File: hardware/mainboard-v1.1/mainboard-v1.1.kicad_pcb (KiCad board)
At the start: 2 copper layers, 86 x 62 mm, 27 parts, among them J1 Conn_01x01, J2 Conn_01x01, J3 Conn_01x03, J4 Conn_01x03, J5 Conn_01x05, SW1 SW_SPDT, SW2 SW_SPST, SW3 SW_SPST, SW4 SW_SPST, SW5 SW_SPST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

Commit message: pcb update for v1.1
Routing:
- net /SERVO1: track 42.3 -> 46.6 mm
- net /SERVO2: track 42.3 -> 41.1 mm
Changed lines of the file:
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@@
     (fp_arc (start 10.726537 -0.155903) (mid 11.428136 -0.857503) (end 12.129736 -0.155903)
       (stroke (width 0.25) (type solid)) (layer "Dwgs.User"))
-    (fp_arc (start 11.740267 -36.934704) (mid 12.447516 -36.641667) (end 12.740267 -35.934303)
+    (fp_arc (start 11.740267 -36.934704) (mid 12.447538 -36.641681) (end 12.740267 -35.934303)
       (stroke (width 0.25) (type solid)) (layer "Dwgs.User"))
     (fp_arc (start 12.716687 22.847905) (mid 12.42365 23.554745) (end 11.716687 23.847504)
@@
   (segment (start 134.5 74.8) (end 136.45 74.8) (width 0.25) (layer "F.Cu") (net 2))
   (via (at 136.5 74.8) (size 0.8) (drill 0.4) (layers "F.Cu" "B.Cu") (net 2))
-  (segment (start 121.81 78.19) (end 121.81 77.94) (width 0.5) (layer "B.Cu") (net 2))
+  (segment (start 126.5 73.25) (end 135.85 73.25) (width 0.5) (layer "B.Cu") (net 2))
+  (segment (start 136.5 73.9) (end 136.5 74.8) (width 0.5) (layer "B.Cu") (net 2))
   (segment (start 114 78) (end 121.62 78) (width 0.5) (layer "B.Cu") (net 2))
-  (segment (start 126.5 73.25) (end 136.25 73.25) (width 0.5) (layer "B.Cu") (net 2))
   (segment (start 121.62 78) (end 121.81 78.19) (width 0.5) (layer "B.Cu") (net 2))
   (segment (start 171 81.25) (end 171 78) (width 0.5) (layer "B.Cu") (net 2))
@@
   (segment (start 125.49 87.25) (end 165 87.25) (width 0.5) (layer "B.Cu") (net 2))
   (segment (start 121.81 83.57) (end 121.81 78.19) (width 0.5) (layer "B.Cu") (net 2))
+  (segment (start 121.81 77.94) (end 126.5 73.25) (width 0.5) (layer "B.Cu") (net 2))
+  (segment (start 121.81 78.19) (end 121.81 77.94) (width 0.5) (layer "B.Cu") (net 2))
   (segment (start 121.81 83.57) (end 125.49 87.25) (width 0.5) (layer "B.Cu") (net 2))
-  (segment (start 136.25 73.25) (end 136.5 73.5) (width 0.5) (layer "B.Cu") (net 2))
-  (segment (start 121.81 77.94) (end 126.5 73.25) (width 0.5) (layer "B.Cu") (net 2))
-  (segment (start 136.5 73.5) (end 136.5 74.8) (width 0.5) (layer "B.Cu") (net 2))
+  (segment (start 135.85 73.25) (end 136.5 73.9) (width 0.5) (layer "B.Cu") (net 2))
   (segment (start 111.5 78) (end 115.282934 81.782934) (width 0.25) (layer "F.Cu") (net 3))
   (segment (start 115.282934 81.782934) (end 123.782934 81.782934) (width 0.25) (layer "F.Cu") (net 3))
@@
   (segment (start 163.5 86) (end 168.5 81) (width 0.25) (layer "F.Cu") (net 5))
   (segment (start 168.5 81) (end 168.5 78) (width 0.25) (layer "F.Cu") (net 5))
-  (segment (start 132.8 74.8) (end 132.75 74.75) (width 0.25) (layer "F.Cu") (net 6))
-  (segment (start 132.75 76) (end 131.97 76.78) (width 0.5) (layer "F.Cu") (net 6))
-  (segment (start 132.75 74.75) (end 132.75 76) (width 0.5) (layer "F.Cu") (net 6))
-  (segment (start 131.97 76.78) (end 131.97 83.57) (width 0.5) (layer "F.Cu") (net 6))
-  (segment (start 133 74.8) (end 132.8 74.8) (width 0.25) (layer "F.Cu") (net 6))
+  (segment (start 132.8 75.9) (end 131.97 76.73) (width 0.5) (layer "F.Cu") (net 6))
+  (segment (start 133 75.7) (end 133 74.8) (width 0.25) (layer "F.Cu") (net 6))
+  (segment (start 132.8 75.9) (end 133 75.7) (width 0.25) (layer "F.Cu") (net 6))
+  (segment (start 131.97 76.73) (end 131.97 83.57) (width 0.5) (layer "F.Cu") (net 6))
   (segment (start 134.5 73) (end 134 73.5) (width 0.25) (layer "F.Cu") (net 7))
   (segment (start 134 73.5) (end 134 74.8) (width 0.25) (layer "F.Cu") (net 7))
-  (segment (start 134 75.30962) (end 137.05 78.35962) (width 0.25) (layer "F.Cu") (net 7))
-  (segment (start 134 74.8) (end 134 75.30962) (width 0.25) (layer "F.Cu") (net 7))
+  (segment (start 134.025 74.825) (end 134.025 75.33462) (width 0.25) (layer "F.Cu") (net 7))
   (segment (start 137.05 78.35962) (end 137.05 83.57) (width 0.25) (layer "F.Cu") (net 7))
+  (segment (start 134 74.8) (end 134.025 74.825) (width 0.25) (layer "F.Cu") (net 7))
   (segment (start 134.5 71.7) (end 134.5 73) (width 0.25) (layer "F.Cu") (net 7))
+  (segment (start 134.025 75.33462) (end 137.05 78.35962) (width 0.25) (layer "F.Cu") (net 7))
   (segment (start 159.49 62.225) (end 159.49 76.26) (width 0.25) (layer "F.Cu") (net 11))
   (segment (start 153.75 80.05) (end 153.75 80.75) (width 1) (layer "F.Cu") (net 11))
@@
   (segment (start 130.25 116.5) (end 130.25 110) (width 0.25) (layer "F.Cu") (net 14))
   (segment (start 129.43 109.18) (end 130.25 110) (width 0.25) (layer "F.Cu") (net 14))
-  (segment (start 133.5 76) (end 133.5 75.622793) (width 0.5) (layer "F.Cu") (net 15))
-  (segment (start 133.5 74.8) (end 133.5 75.5) (width 0.25) (layer "F.Cu") (net 15))
-  (segment (start 134.51 77.01) (end 133.5 76) (width 0.5) (layer "F.Cu") (net 15))
-  (segment (start 134.51 83.57) (end 134.51 77.01) (width 0.5) (layer "F.Cu") (net 15))
+  (segment (start 134.51 76.76) (end 134.51 83.57) (width 0.5) (layer "F.Cu") (net 15))
+  (segment (start 133.75 76) (end 134.51 76.76) (width 0.5) (layer "F.Cu") (net 15))
+  (segment (start 133.75 76) (end 133.5 75.75) (width 0.25) (layer "F.Cu") (net 15))
+  (segment (start 133.5 75.75) (end 133.5 74.8) (width 0.25) (layer "F.Cu") (net 15))
   (segment (start 139.59 79.41) (end 151.08 67.92) (width 0.5) (layer "F.Cu") (net 16))
   (segment (start 139.59 83.57) (end 139.59 79.41) (width 0.5) (layer "F.Cu") (net 16))
   (segment (start 151.08 67.92) (end 151.08 64) (width 0.5) (layer "F.Cu") (net 16))
-  (segment (start 163.75 60) (end 164.57 60.82) (width 0.5) (layer "B.Cu") (net 16))
-  (segment (start 164.57 60.82) (end 164.57 62.225) (width 0.5) (layer "B.Cu") (net 16))
-  (segment (start 153.25 60) (end 163.75 60) (width 0.5) (layer "B.Cu") (net 16))
-  (segment (start 151.08 62.17) (end 153.25 60) (width 0.5) (layer "B.Cu") (net 16))
-  (segment (start 151.08 64) (end 151.08 62.17) (width 0.5) (layer "B.Cu") (net 16))
+  (segment (start 152.78 65.7) (end 163.1 65.7) (width 0.5) (layer "B.Cu") (net 16))
+  (segment (start 164.57 64.23) (end 164.57 62.225) (width 0.5) (layer "B.Cu") (net 16))
+  (segment (start 163.1 65.7) (end 164.57 64.23) (width 0.5) (layer "B.Cu") (net 16))
+  (segment (start 151.08 64) (end 152.78 65.7) (width 0.5) (layer "B.Cu") (net 16))
   (segment (start 136.5 71.25) (end 136 70.75) (width 0.25) (layer "F.Cu") (net 17))
   (segment (start 133.9 64.1) (end 133.9 71.55) (width 0.5) (layer "F.Cu") (net 17))
@@
   (segment (start 133.5 71.7) (end 134 71.7) (width 0.25) (layer "F.Cu") (net 17))
   (via (at 136 70.75) (size 0.8) (drill 0.4) (layers "F.Cu" "B.Cu") (net 17))
-  (segment (start 155.75 70.75) (end 162.03 64.47) (width 0.25) (layer "B.Cu") (net 17))
-  (segment (start 136 70.75) (end 155.75 70.75) (width 0.25) (layer "B.Cu") (net 17))
-  (segment (start 162.03 64.47) (end 162.03 62.225) (width 0.25) (layer "B.Cu") (net 17))
+  (segment (start 136 65.7) (end 141.8 59.9) (width 0.25) (layer "B.Cu") (net 17))
+  (segment (start 162.03 61.03) (end 162.03 62.225) (width 0.25) (layer "B.Cu") (net 17))
+  (segment (start 136 70.75) (end 136 65.7) (width 0.25) (layer "B.Cu") (net 17))
+  (segment (start 160.9 59.9) (end 162.03 61.03) (width 0.25) (layer "B.Cu") (net 17))
+  (segment (start 141.8 59.9) (end 160.9 59.9) (width 0.25) (layer "B.Cu") (net 17))
   (segment (start 100.75 95.75) (end 101.5 95) (width 1.5) (layer "F.Cu") (net 19))
   (segment (start 104.5 112) (end 100.75 108.25) (width 1.5) (layer "F.Cu") (net 19))

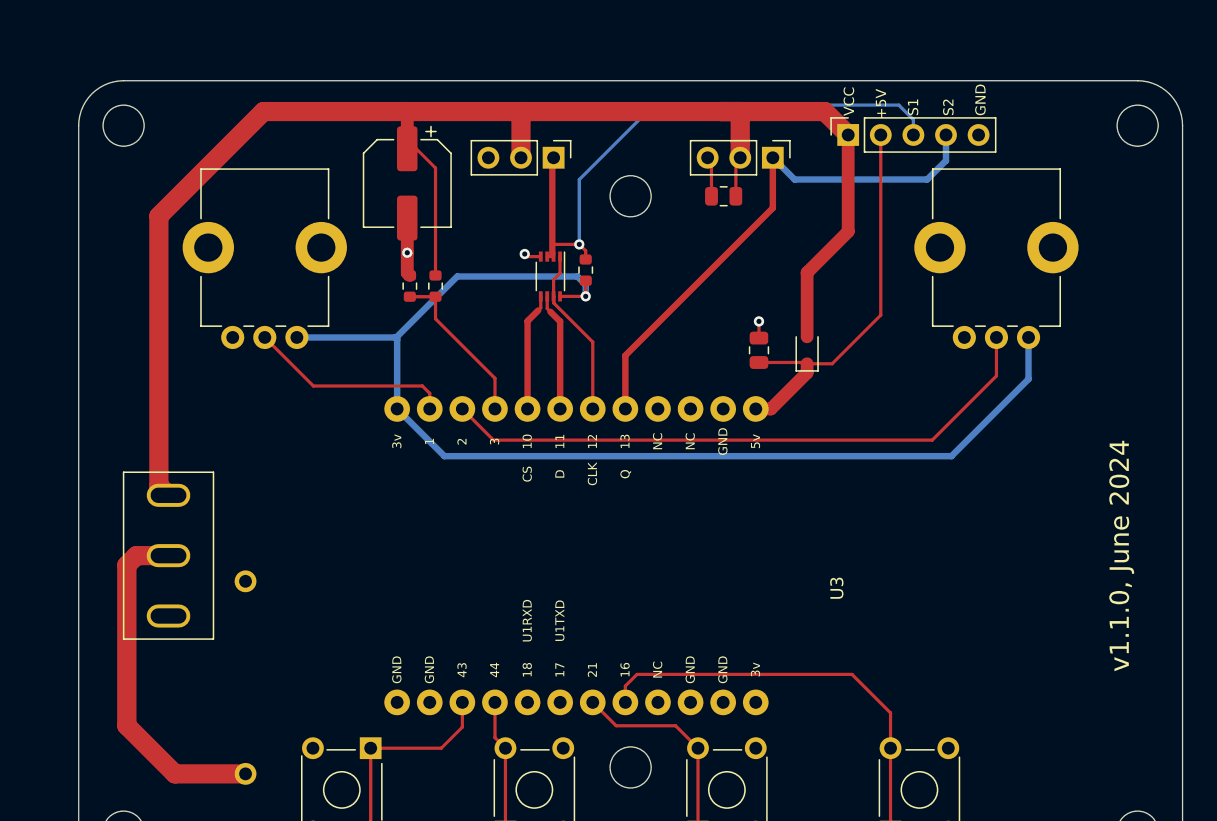
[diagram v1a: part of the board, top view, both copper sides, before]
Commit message: updating firmware for v 1.1
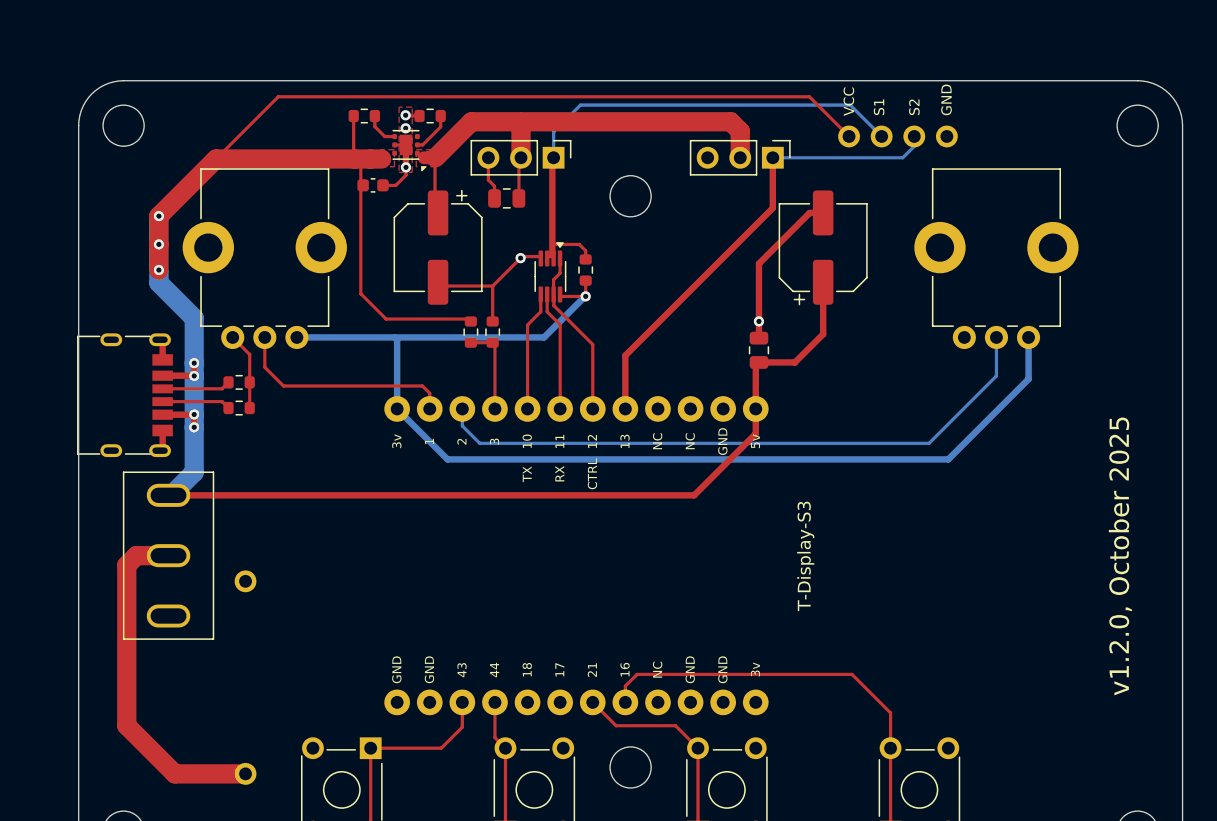
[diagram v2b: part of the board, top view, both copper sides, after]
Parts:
- removed D1: D_Schottky, Diode_SMD:D_SOD-323
- added C1: 22uF, Capacitor_SMD:C_0805_2012Metric, F.Cu at (130.3, 67.2)
- added C2: 220uF, Capacitor_SMD:CP_Elec_6.3x7.7, F.Cu at (155.0, 71.0)
- added J6: Conn_01x04, shurik-personal:connector-4p-generic-nosilk, F.Cu at (157.0, 62.3)
- added R4: 120k, Resistor_SMD:R_0603_1608Metric, F.Cu at (124.4, 60.8)
- added R5: 120k, Resistor_SMD:R_0603_1608Metric, F.Cu at (119.2, 60.8)
- added R6: 5.1K, Resistor_SMD:R_0603_1608Metric, F.Cu at (109.5, 83.5)
- added R7: 5.1K, Resistor_SMD:R_0603_1608Metric, F.Cu at (109.5, 81.5)
- added U1: TPS25200, Package_SON:WSON-6-1EP_2x2mm_P0.65mm_EP1x1.6mm, F.Cu at (122.5, 63.0)
- C3: value 22uF -> 100nF; footprint Capacitor_SMD:C_0805_2012Metric -> Capacitor_SMD:C_0603_1608Metric
- J5: value Conn_01x05 -> USB_C_Receptacle_PowerOnly_6P; footprint Connector_PinSocket_2.54mm:PinSocket_1x05_P2.54mm_Vertical -> shurik-personal:USB_C_Receptacle_Korean_Hroparts-31-M-17
- moved J5 60.9 mm to (99.5, 82.5), turned to -90 degrees
- moved C3 27.3 mm to (119.9, 66.2), turned to 0 degrees
- moved R2 7.38 mm to (129.3, 77.6)
- moved C5 5.55 mm to (125.0, 71.0)
- moved R1 4.52 mm to (127.6, 77.6)
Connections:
- C4 pad 1: +5V -> VCC
- C5 pad 1: VCC -> /SERVO_POWER
- J3 pad 2: VCC -> /SERVO_POWER
- J4 pad 2: VCC -> /SERVO_POWER
- U3 pad 12: +5V -> VCC
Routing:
- net VCC: track 122.5 -> 193.1 mm, vias 0 -> 7
- net /SERVO_POWER: track 0.00 -> 38.4 mm
- net GND: track 9.89 -> 42.5 mm, vias 3 -> 5
- net +5V: track 30.9 -> 0.00 mm
- net /VSENSE: track 12.7 -> 6.69 mm
- net /SERVO1: track 46.6 -> 40.9 mm, vias 1 -> 0
- net Net-(J5-CC2): track 0.00 -> 5.34 mm
- net Net-(J5-CC1): track 0.00 -> 5.34 mm
- net /SERVO2: track 41.1 -> 36.5 mm
- net Net-(U1-ILIM): track 0.00 -> 3.24 mm
- net Net-(U1-EN): track 0.00 -> 2.68 mm
- net +3.3V: track 91.0 -> 89.1 mm
- net /POT1: track 15.9 -> 17.2 mm
- net /POT2: track 47.7 -> 48.7 mm
- added copper zone on F.Cu, net /SERVO_POWER
- added copper zone on F.Cu, net GND
- added copper zone on F.Cu, net VCC
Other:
- board text added: "v1.2.0, October 2025"
- board text removed: "+5V"
- board text removed: "v1.1.0, June 2024"
